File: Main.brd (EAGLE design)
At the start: 100 x 80 mm, 29 parts, among them Q1 IRF9530, U1 L298, U2 LM 1084 IT5,0, U3 LM 1084 IT3,3, U4 L298, X1 Motors, X2 PIRs, X3 Battery

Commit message: some cleanup
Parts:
- moved D1 1.27 mm to (91.4, 50.8), turned to 0 degrees
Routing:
- net GND: track 411.9 -> 0.00 mm, vias 3 -> 0
- net +12V: track 257.6 -> 0.00 mm, vias 2 -> 0
- net +5V: track 239.7 -> 0.00 mm, vias 1 -> 0
- net ML_OUT_A: track 165.1 -> 0.00 mm, vias 1 -> 0
- net ML_OUT_B: track 153.3 -> 0.00 mm, vias 2 -> 0
- net MR_OUT_B: track 120.6 -> 0.00 mm
- net MR_B: track 109.9 -> 0.00 mm, vias 1 -> 0
- net MR_A: track 102.3 -> 0.00 mm
- net ML_PWM: track 100.3 -> 0.00 mm
- net ML_B: track 85.2 -> 0.00 mm, vias 1 -> 0
- net ML_A: track 84.0 -> 0.00 mm
- net MR_PWM: track 76.2 -> 0.00 mm, vias 1 -> 0
- net MR_OUT_A: track 71.8 -> 0.00 mm
- net N$1: track 34.9 -> 0.00 mm
- net +3.3V: track 29.5 -> 0.00 mm
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
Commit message: fuses
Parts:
- removed C3: 10uF Tant., rcl:C025-040X050
- added F1: PFRA 600, Sicherungselemente:SE250
- added F2: PTC194600-110, _hhn_PtcFuses_Siba_r500:1820
- added F3, F4, F5, F6: PTC194600-150, _hhn_PtcFuses_Siba_r500:1820
- moved D9 16.1 mm to (49.5, 43.2)
- moved D11 15.2 mm to (34.3, 30.5)
- moved D6 13.5 mm to (87.6, 17.8)
- moved D5 12.0 mm to (87.6, 33.0)
- moved D4 11.5 mm to (30.5, 41.9)
- moved C4 10.9 mm to (95.2, 15.2), turned to 0 degrees
- moved R1 8.52 mm to (90.2, 43.2)
- moved X2 6.48 mm to (50.8, 59.7)
- moved D10 6.35 mm to (25.4, 52.1)
- moved C6 5.39 mm to (77.5, 74.9)
- moved C5 4.58 mm to (88.9, 67.3), turned to 0 degrees
- moved C2 4.58 mm to (83.8, 74.9)
- moved C8 4.58 mm to (82.5, 57.1), turned to 0 degrees
- moved X3 4.02 mm to (90.2, 73.7)
- moved C7 3.59 mm to (87.6, 62.2), turned to 0 degrees
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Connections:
- new net N$26: F4.2, X1.3
- new net N$34: F5.2, X1.5
- new net N$36: F6.2, X1.7
- new net N$4: F1.1, X3.1
- new net N$5: F2.1, SV1.2, SV1.4
- new net N$7: F3.2, X1.1
- net +12V: no longer C3.1
- net +5V: now also F2.2; no longer SV1.2, SV1.4
- net GND: no longer C3.2
- net ML_OUT_A: now also F3.1, F4.1; no longer X1.1, X1.3
- net MR_OUT_A: now also F5.1, F6.1; no longer X1.5, X1.7
- net N$1: now also F1.2; no longer X3.1
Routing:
- net GND: track 0.00 -> 356.2 mm, vias 0 -> 2
- net +5V: track 0.00 -> 253.2 mm, vias 0 -> 6
- net +12V: track 0.00 -> 249.7 mm, vias 0 -> 3
- net ML_OUT_A: track 0.00 -> 154.8 mm, vias 0 -> 4
- net ML_OUT_B: track 0.00 -> 131.2 mm, vias 0 -> 4
- net ML_A: track 0.00 -> 110.9 mm, vias 0 -> 2
- net MR_OUT_B: track 0.00 -> 110.3 mm, vias 0 -> 3
- net ML_PWM: track 0.00 -> 103.8 mm, vias 0 -> 3
- net MR_A: track 0.00 -> 100.5 mm
- net ML_B: track 0.00 -> 84.4 mm
- net MR_PWM: track 0.00 -> 79.8 mm
- net MR_OUT_A: track 0.00 -> 78.6 mm, vias 0 -> 2
- net MR_B: track 0.00 -> 76.3 mm, vias 0 -> 1
- net N$5: track 0.00 -> 68.5 mm, vias 0 -> 1
- net N$1: track 0.00 -> 24.4 mm
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
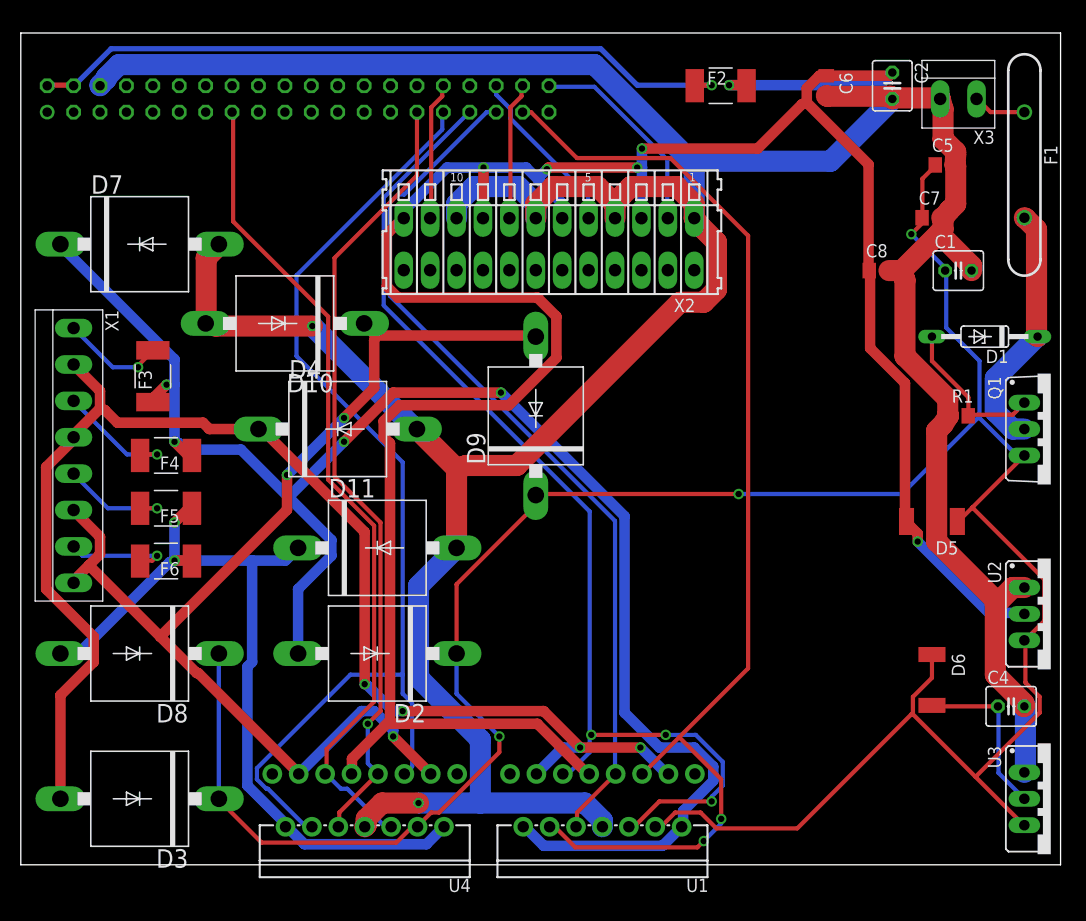
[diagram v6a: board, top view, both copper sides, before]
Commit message: added 2 ultrasonic sensors
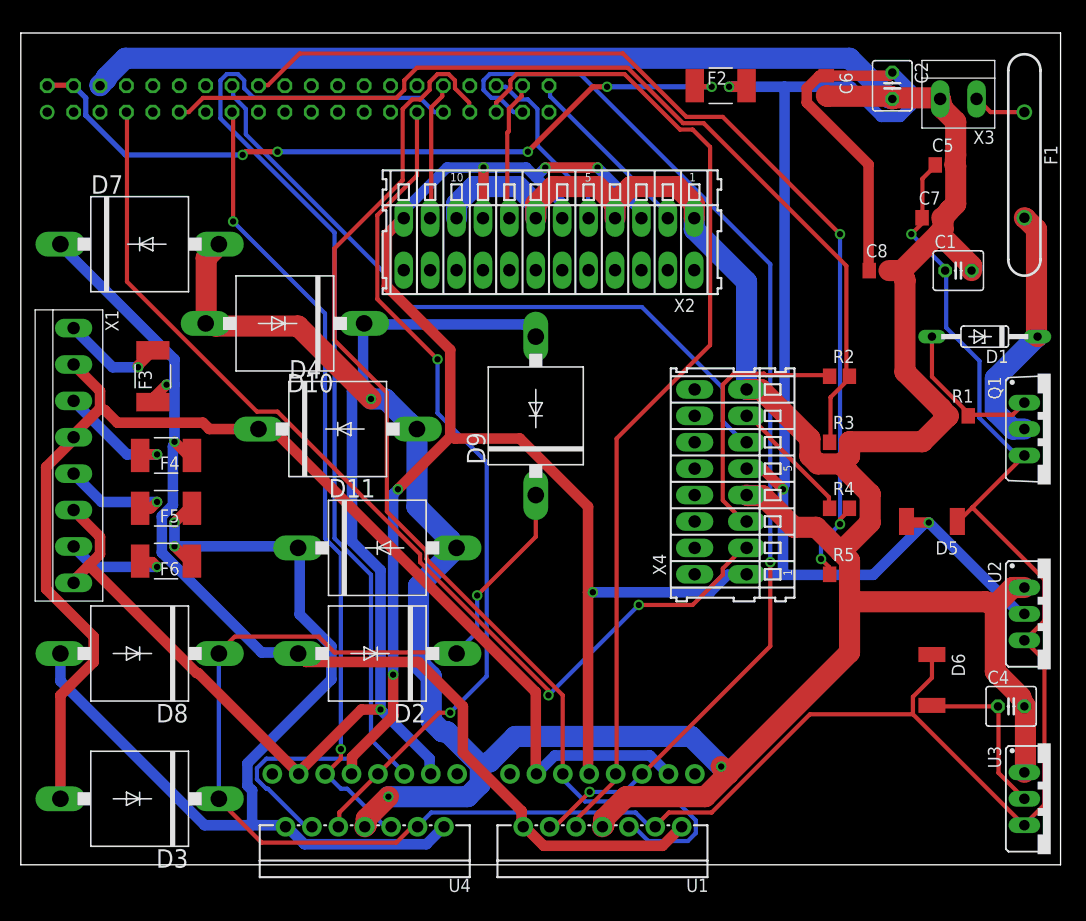
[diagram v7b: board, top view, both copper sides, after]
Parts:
- added R2, R4: 330, resistor:R0805
- added R3, R5: 470, resistor:R0805
- added X4: (no value), con-wago:233-508
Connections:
- removed net N$14: SV1.18
- removed net N$15: SV1.16
- removed net N$22: SV1.7
- removed net N$24: SV1.11
- new net N$16: R2.1, X4.B3
- new net N$35: R4.1, X4.B7
- new net USM_A_ECHO: R2.2, R3.1, SV1.11
- new net USM_A_TRIG: SV1.7, X4.B2
- new net USM_B_ECHO: R4.2, R5.1, SV1.18
- new net USM_B_TRIG: SV1.16, X4.B6
- net +5V: now also X4.B1, X4.B5
- net GND: now also R3.2, R5.2, X4.B4, X4.B8
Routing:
- net USM_B_ECHO: track 0.00 -> 100.2 mm, vias 0 -> 3
- net USM_A_TRIG: track 0.00 -> 99.4 mm, vias 0 -> 2
- net USM_A_ECHO: track 0.00 -> 92.4 mm
- net USM_B_TRIG: track 0.00 -> 68.0 mm
- net GND: track 356.2 -> 420.0 mm, vias 2 -> 3
- net ML_OUT_A: track 154.8 -> 105.9 mm, vias 4 -> 2
- net +5V: track 253.2 -> 296.5 mm, vias 6 -> 9
- net N$16: track 0.00 -> 25.1 mm
- net MR_OUT_A: track 78.6 -> 97.0 mm
- net +12V: track 249.7 -> 232.1 mm, vias 3 -> 2
- net MR_A: track 100.5 -> 118.0 mm
- net N$35: track 0.00 -> 12.5 mm
- net ML_B: track 84.4 -> 96.7 mm
- net ML_OUT_B: track 131.2 -> 123.4 mm, vias 4 -> 0
- net ML_PWM: track 103.8 -> 110.1 mm, vias 3 -> 0
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
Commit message: ?
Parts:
- X4: value (none) -> Ultra Sonics
- moved D3 3.81 mm to (11.4, 10.2)
- moved D11 3.81 mm to (30.5, 30.5)
- moved D9 1.27 mm to (48.3, 43.2)
- moved D2 1.27 mm to (33.0, 20.3)
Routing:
- net GND: track 420.0 -> 0.00 mm, vias 3 -> 0
- net +5V: track 296.5 -> 0.00 mm, vias 9 -> 0
- net +12V: track 232.1 -> 0.00 mm, vias 2 -> 0
- net ML_OUT_B: track 123.4 -> 0.00 mm
- net MR_A: track 118.0 -> 0.00 mm
- net MR_OUT_B: track 112.2 -> 0.00 mm, vias 1 -> 0
- net ML_PWM: track 110.1 -> 0.00 mm
- net ML_A: track 106.2 -> 0.00 mm, vias 2 -> 0
- net ML_OUT_A: track 105.9 -> 0.00 mm, vias 2 -> 0
- net USM_B_ECHO: track 100.2 -> 0.00 mm, vias 3 -> 0
- net USM_A_TRIG: track 99.4 -> 0.00 mm, vias 2 -> 0
- net MR_OUT_A: track 97.0 -> 0.00 mm, vias 2 -> 0
- net ML_B: track 96.7 -> 0.00 mm
- net USM_A_ECHO: track 92.4 -> 0.00 mm
- net MR_B: track 81.2 -> 0.00 mm, vias 2 -> 0
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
